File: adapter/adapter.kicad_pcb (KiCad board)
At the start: 2 copper layers, 93.6 x 71.8 mm, 44 parts, among them J10 Ribbon, J11 Ribbon, J12 Ribbon, J13 serial, J7 trackball, J8 trackball, J9 Ribbon, SW1 SW_SPST, SW2 SW_SPST, SW3 SW_SPDT, SW4 SW_SPDT, U1 eliteC, U2 eliteC

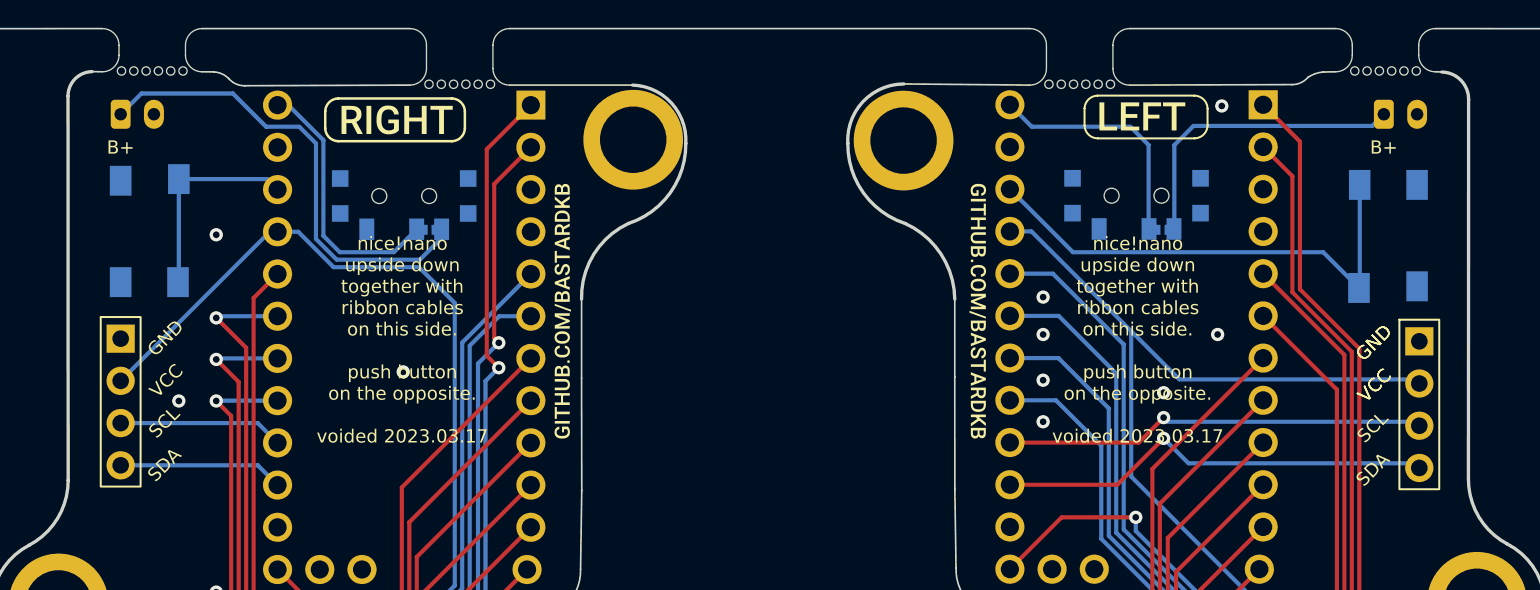
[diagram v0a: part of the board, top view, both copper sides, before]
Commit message: updated schematic
- updated schematic to reflect pcb changes
- removed rgb, serial, swapped spi pinout, updated battery footprint
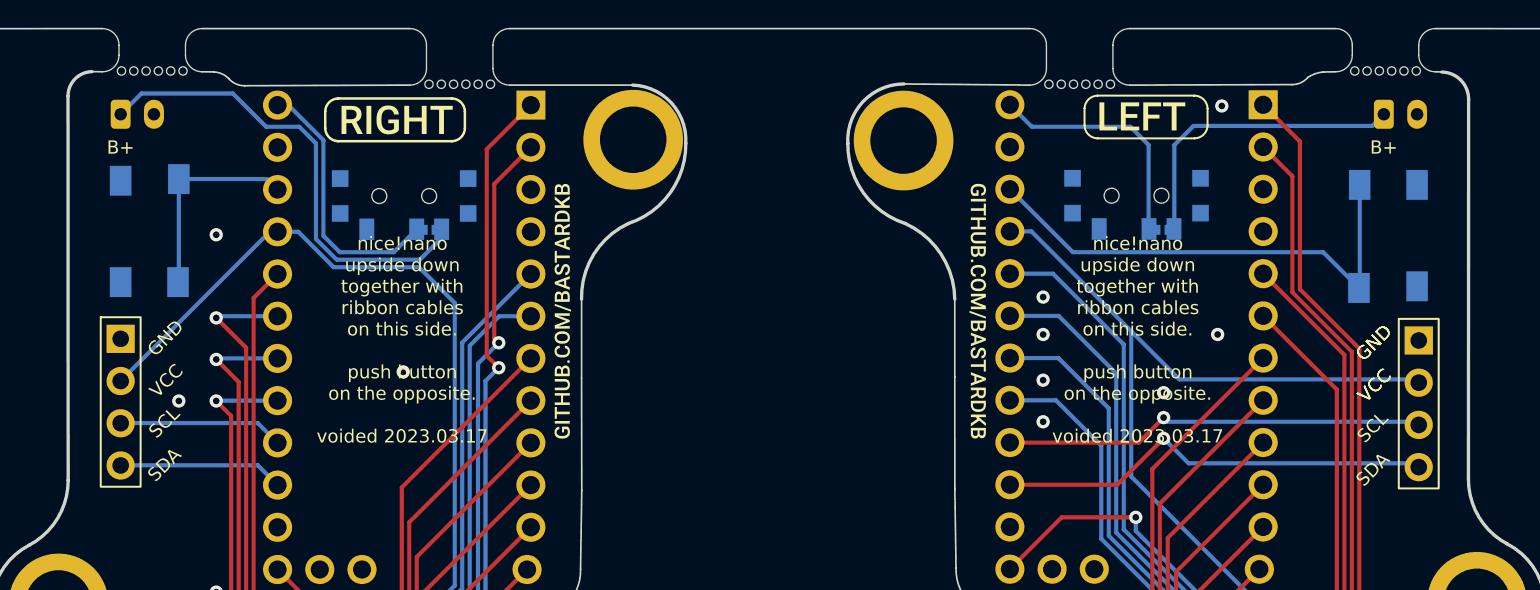
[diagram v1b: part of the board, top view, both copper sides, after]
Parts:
- removed the J13 at (194.6, 83.4)
- removed the J13 at (116.5, 83.2)
- removed the REF** at (192.5, 69.8)
- removed the REF** at (116.5, 69.8)
- added J13: serial, Library:PinHeader_1x04_P2.54mm_Vertical, F.Cu at (194.6, 83.4)
- added J14: serial, Library:PinHeader_1x04_P2.54mm_Vertical, F.Cu at (116.5, 83.3)
- added J3: battery charge, Connector_JST:JST_PH_B2B-PH-K_1x02_P2.00mm_Vertical, F.Cu at (116.5, 69.8)
- added J6: battery charge, Connector_JST:JST_PH_B2B-PH-K_1x02_P2.00mm_Vertical, F.Cu at (192.5, 69.8)
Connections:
- U1 pad 14: (no net) -> unconnected-(U1-B2-Pad14)
- U1 pad 28: (no net) -> unconnected-(U1-F1-Pad28)
- U1 pad 29: (no net) -> unconnected-(U1-F0-Pad29)
- U2 pad 14: (no net) -> unconnected-(U2-B2-Pad14)
- U2 pad 28: (no net) -> unconnected-(U2-F1-Pad28)
- U2 pad 29: (no net) -> unconnected-(U2-F0-Pad29)

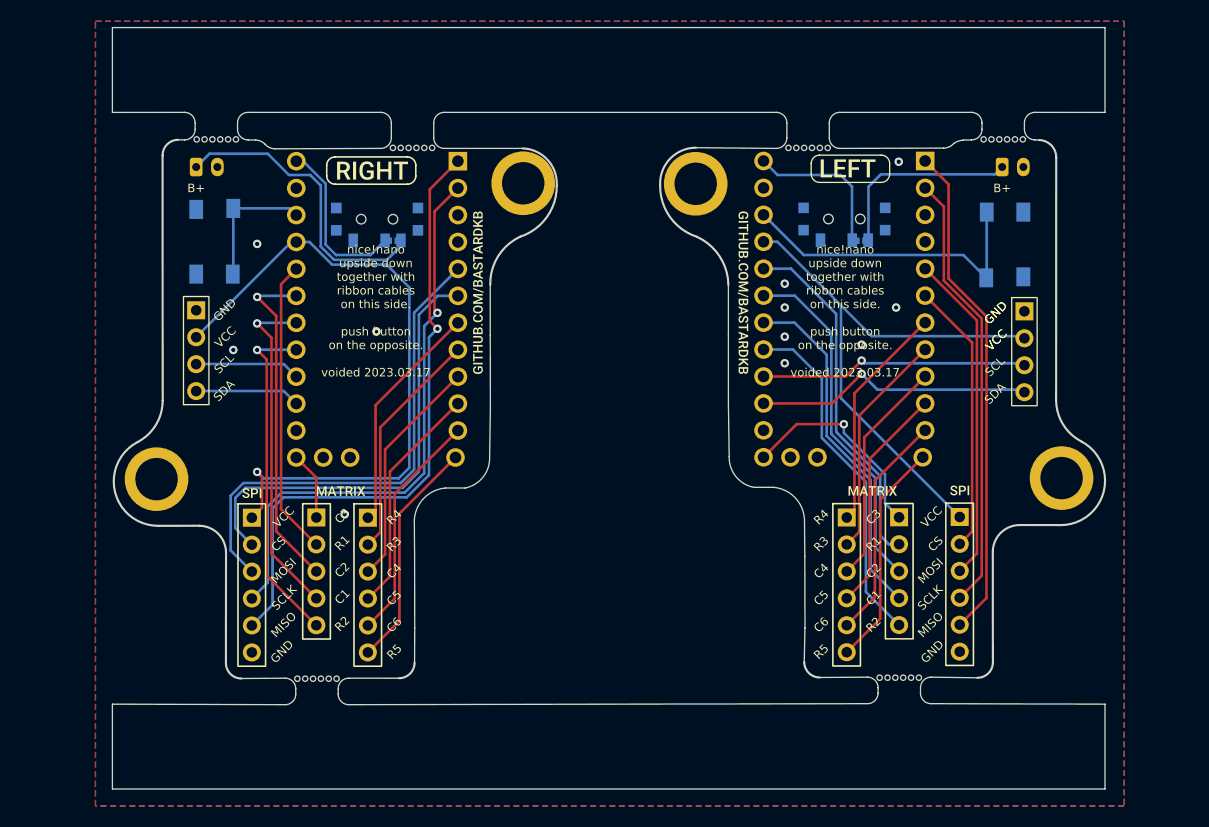
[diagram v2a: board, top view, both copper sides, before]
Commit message: Revert to old board outlines
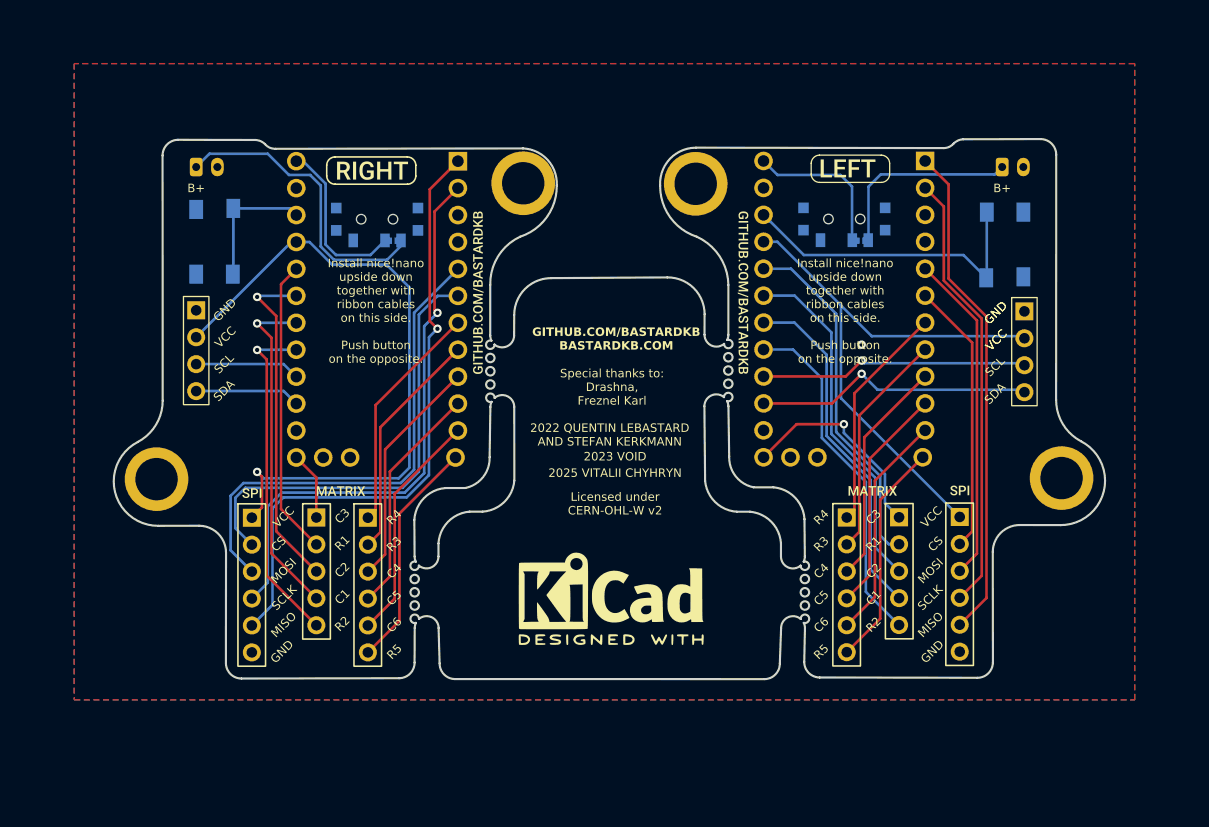
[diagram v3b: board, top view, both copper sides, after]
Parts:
- removed REF** (x6): mousebites 2mm, marbastlib-various:mousebites_2.5mm
- added G***: LOGO, LOGO, F.Cu at (155.5, 110.5)
- added G***: LOGO, LOGO, B.Cu at (155.8, 110.5)
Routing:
- net GND: vias 11 -> 1
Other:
- board size 93.6 x 71.8 mm -> 93.5 x 50.9 mm
- board text added: "2022 QUENTIN LEBASTARD AND STEFAN KERKMANN"
- board text added: "2023 VOID"
- board text added: "2025 VITALII CHYHRYN"
- board text added: "GITHUB.COM/BASTARDKB BASTARDKB.COM"
- board text added: "Install nice!nano upside down together with ribbon cables on this side. Push button on the opposite."
- board text added: "Licensed under CERN-OHL-W v2"
- board text added: "Special thanks to: Drashna, Freznel Karl"
- board text removed: "nice!nano upside down together with ribbon cables on this side. push button on the opposite. voided 2023.03.17"

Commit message: Move reset button and power switch
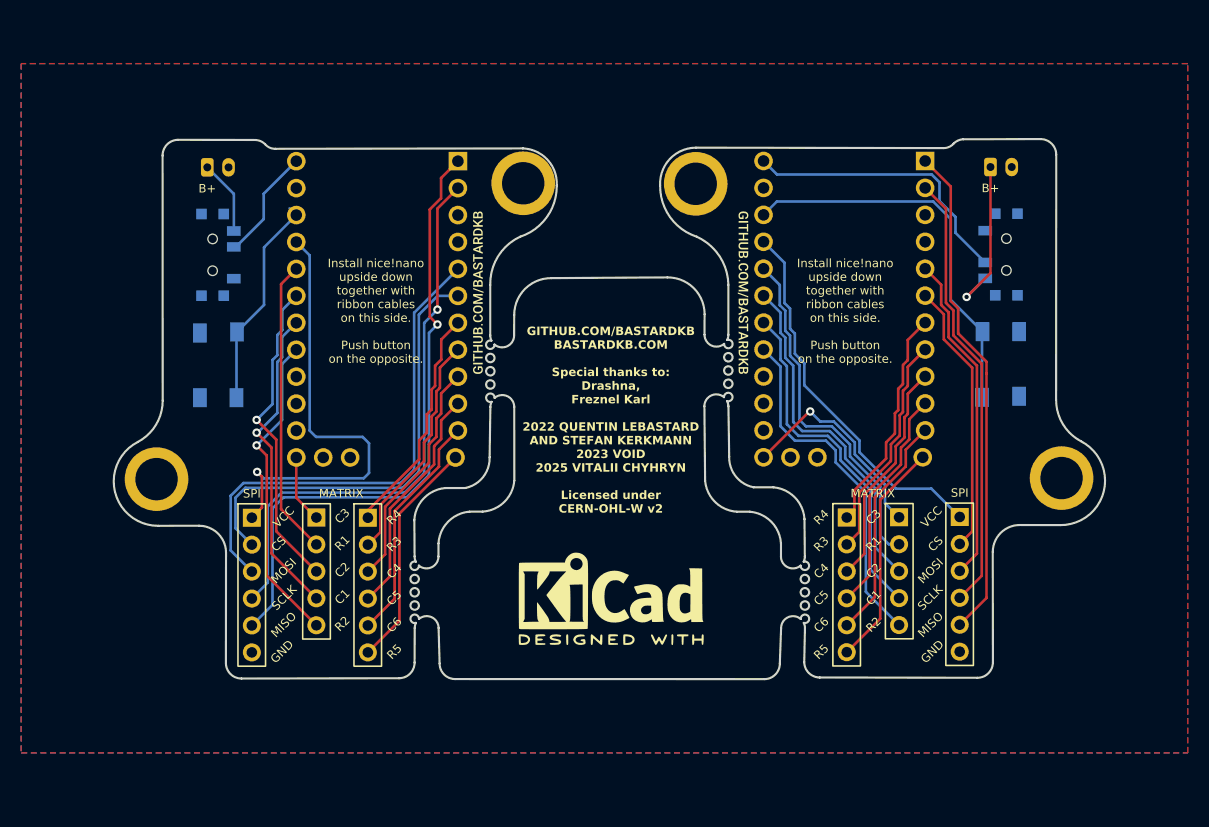
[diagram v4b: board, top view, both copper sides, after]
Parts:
- removed J13, J14: serial, Library:PinHeader_1x04_P2.54mm_Vertical
- removed JP1, JP2: Jumper_2_Open, Library:power_switch_jumper
- removed kibuzzard-61F01940 (x4): G***, kibuzzard-61F01940
- removed kibuzzard-61F01957 (x4): G***, kibuzzard-61F01957
- removed kibuzzard-61F01B61 (x2): G***, kibuzzard-61F01B61
- removed kibuzzard-6208EFFE (x2): G***, kibuzzard-6208EFFE
- removed kibuzzard-620B8593 (x2): G***, kibuzzard-620B8593
- J3, J6: value battery charge -> Battery charge
- J7, J8: value trackball -> Trackball
- moved SW3 15.9 mm to (118.0, 78.0), turned to 90 degrees
- moved SW4 15.6 mm to (192.9, 78.0), turned to -90 degrees
- moved SW1 11.7 mm to (118.5, 88.4)
- moved SW2 11.3 mm to (192.4, 88.4)
- moved J6 1.10 mm to (191.4, 69.8)
- moved J3 1.05 mm to (117.5, 69.8)
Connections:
- J7 pad 1: +5V -> +5V_1
- J8 pad 1: +5V -> +5V_2
- U1 pad 15: sda_l -> unconnected-(U1-B3-Pad15)
- U1 pad 16: scl_l -> unconnected-(U1-B1-Pad16)
- U1 pad 21: +5V -> +5V_1
- U2 pad 15: sda_r -> unconnected-(U2-B3-Pad15)
- U2 pad 16: scl_r -> unconnected-(U2-B1-Pad16)
- U2 pad 21: +5V -> +5V_2
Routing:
- net +5V: track 115.5 -> 0.00 mm, vias 1 -> 0
- net +5V_1: track 0.00 -> 43.6 mm, vias 0 -> 1
- net +5V_2: track 0.00 -> 35.6 mm
- net sda_r: track 26.5 -> 0.00 mm, vias 1 -> 0
- net scl_r: track 25.4 -> 0.00 mm, vias 1 -> 0
- net bat_sw_l: track 28.4 -> 7.04 mm
- net bat_r: track 14.4 -> 26.8 mm
- net scl_l: track 9.94 -> 0.00 mm
- net sda_l: track 9.94 -> 0.00 mm
- net Rst: track 12.4 -> 20.4 mm
- net Rst2: track 29.7 -> 37.0 mm
- net bat_l: track 16.0 -> 11.3 mm
- net bat_sw_r: track 18.4 -> 15.8 mm, vias 0 -> 1
- net row2_l: track 32.0 -> 29.9 mm
- net col2_l: track 31.9 -> 29.9 mm
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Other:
- board text added: "GITHUB.COM/BASTARDKB BASTARDKB.COM Special thanks to: Drashna, Freznel Karl 2022 QUENTIN LEBASTARD AND STEFAN KERKMANN 2023 VOID 2025 VITALII CHYHRYN Licensed under CERN-OHL-W v2"
- board text added: "LEFT"
- board text added: "MATRIX"
- board text added: "OFF / ON"
- board text added: "RESET"
- board text added: "RIGHT"
- board text added: "SPI"
- board text removed: "2022 QUENTIN LEBASTARD AND STEFAN KERKMANN"
- board text removed: "2023 VOID"
- board text removed: "2025 VITALII CHYHRYN"
- board text removed: "GITHUB.COM/BASTARDKB BASTARDKB.COM"
- board text removed: "Licensed under CERN-OHL-W v2"
- board text removed: "SCL"
- board text removed: "SDA"
- board text removed: "Special thanks to: Drashna, Freznel Karl"
- board text removed: "n!n HOLDER 0.1"
